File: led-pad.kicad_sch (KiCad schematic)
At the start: 10 parts, among them J1 Conn_01x04_Socket, J2 Conn_01x06_Socket

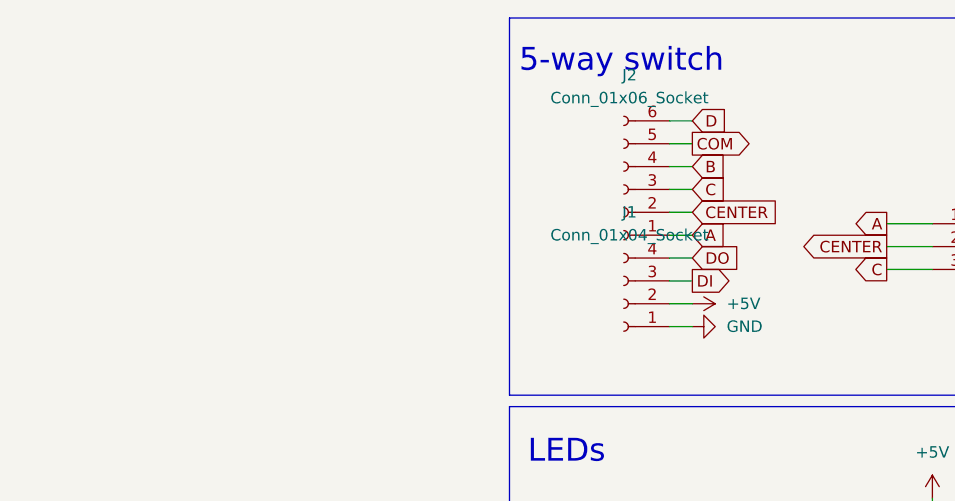
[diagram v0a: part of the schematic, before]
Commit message: reworking for ffc connector, adding step file
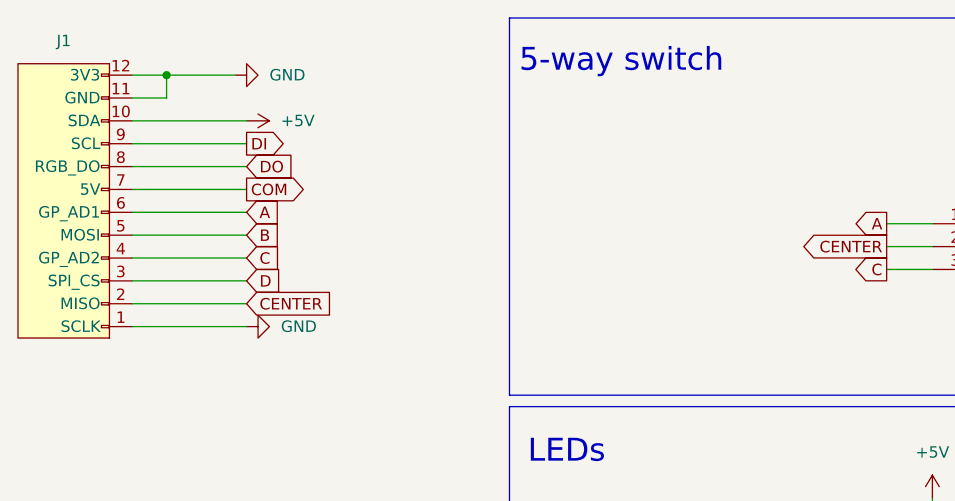
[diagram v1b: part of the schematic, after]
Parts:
- removed J1: Conn_01x04_Socket, Connector_PinSocket_1.27mm:PinSocket_1x04_P1.27mm_Vertical, symbol Connector:Conn_01x04_Socket
- removed J2: Conn_01x06_Socket, Connector_PinSocket_1.27mm:PinSocket_1x06_P1.27mm_Vertical, symbol Connector:Conn_01x06_Socket
- added J1: vik-module-connector, kicad-libraries:FFC-SMD_FFC05001-12SBA124W5M, symbol vik:vik-module-connector
- S1: footprint SKRHAAE010 -> kicad-libraries:SW-SMD_SKRHACE010
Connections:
- net +5V: now also J1.10 (SDA)
- net A: now also J1.6 (GP_AD1)
- net B: now also J1.5 (MOSI)
- net C: now also J1.4 (GP_AD2)
- net CENTER: now also J1.2 (MISO)
- net COM: now also J1.7 (5V)
- net D: now also J1.3 (SPI_CS)
- net DI: now also J1.9 (SCL)
- net DO: now also J1.8 (RGB_DO)
- net GND: now also J1.1 (SCLK), J1.11 (GND), J1.12 (3V3)
